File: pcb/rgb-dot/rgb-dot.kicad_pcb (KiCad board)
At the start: 2 copper layers, 7.6 x 8.9 mm, 4 parts, among them J1 HEADER-1x03, J2 HEADER-1x03, U1 WS2812B

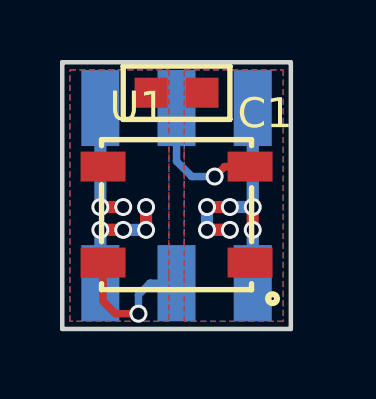
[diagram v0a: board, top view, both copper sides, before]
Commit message: Updated PCB pc-01 pc-02, Added display base pcb (pc-03, pc-04)
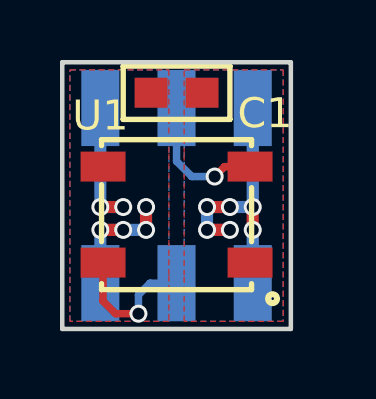
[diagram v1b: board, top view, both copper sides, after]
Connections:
- net Net-(J1-Pad2) renamed /DIN
- net Net-(J2-Pad2) renamed /DOUT
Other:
- board text added: "+"
- board text added: "-"
- board text added: "O-I"
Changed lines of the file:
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@@
-(kicad_pcb (version 4) (host pcbnew "(2015-05-27 BZR 5688)-product")
+(kicad_pcb (version 4) (host pcbnew "(2015-08-16 BZR 6095)-product")
   (general
     (links 8)
     (no_connects 0)
-    (area 142.936476 96.947 154.243524 112.042)
+    (area 144.704999 99.746999 152.475001 108.787001)
     (thickness 0.8)
-    (drawings 14)
+    (drawings 17)
     (tracks 38)
     (zones 0)
@@
   (net 0 "")
   (net 1 +5V)
-  (net 2 "Net-(J1-Pad2)")
-  (net 3 GND)
-  (net 4 "Net-(J2-Pad2)")
+  (net 2 GND)
+  (net 3 /DIN)
+  (net 4 /DOUT)
   (net_class Default "This is the default net class."
     (clearance 0.254)
@@
     (uvia_dia 0.3)
     (uvia_drill 0.1)
-    (add_net "Net-(J1-Pad2)")
-    (add_net "Net-(J2-Pad2)")
+    (add_net /DIN)
+    (add_net /DOUT)
   )
   (net_class Power ""
@@
       (net 1 +5V))
     (pad 2 smd rect (at 0 0) (size 1.27 2.54) (layers B.Cu B.Paste B.Mask)
-      (net 2 "Net-(J1-Pad2)"))
+      (net 3 /DIN))
     (pad 3 smd rect (at 2.54 0) (size 1.27 2.54) (layers B.Cu B.Paste B.Mask)
-      (net 3 GND))
+      (net 2 GND))
   )
   (module Conn-Wire-Pads:WP-50mil-1x03 (layer B.Cu)
@@
       (net 1 +5V))
     (pad 2 smd rect (at 0 0) (size 1.27 2.54) (layers B.Cu B.Paste B.Mask)
-      (net 4 "Net-(J2-Pad2)"))
+      (net 4 /DOUT))
     (pad 3 smd rect (at 2.54 0) (size 1.27 2.54) (layers B.Cu B.Paste B.Mask)
-      (net 3 GND))
+      (net 2 GND))
   )
   (module SMT:LED-5050 (layer F.Cu)
     (at 148.59 104.902)
-    (fp_text reference U1 (at -1.3 -3.6) (layer F.SilkS)
+    (fp_text reference U1 (at -2.54 -3.302) (layer F.SilkS)
       (effects (font (size 1 1) (thickness 0.18)))
     )
@@
     (fp_line (start -2.5 -1) (end -2.5 0.9) (layer F.SilkS) (width 0.18))
     (pad 2 smd rect (at -2.45 1.6) (size 1.5 1) (layers F.Cu F.Paste F.Mask)
-      (net 4 "Net-(J2-Pad2)"))
+      (net 4 /DOUT))
     (pad 3 smd rect (at 2.45 1.6) (size 1.5 1) (layers F.Cu F.Paste F.Mask)
-      (net 3 GND))
+      (net 2 GND))
     (pad 4 smd rect (at 2.45 -1.6) (size 1.5 1) (layers F.Cu F.Paste F.Mask)
-      (net 2 "Net-(J1-Pad2)"))
+      (net 3 /DIN))
     (pad 1 smd rect (at -2.45 -1.6) (size 1.5 1) (layers F.Cu F.Paste F.Mask)
       (net 1 +5V))
@@
     (fp_line (start -1.778 0.889) (end -1.778 -0.889) (layer F.SilkS) (width 0.18))
     (pad 1 smd rect (at -0.85 0 180) (size 1.1 1) (layers F.Cu F.Paste F.Mask)
-      (net 3 GND))
+      (net 2 GND))
     (pad 2 smd rect (at 0.85 0 180) (size 1.1 1) (layers F.Cu F.Paste F.Mask)
       (net 1 +5V))
@@
       (rotate (xyz 0 0 0))
     )
+  )
+  (gr_text - (at 151.13 103.505) (layer B.SilkS)
+    (effects (font (size 1.5 1.5) (thickness 0.3)) (justify mirror))
+  )
+  (gr_text + (at 146.05 103.505) (layer B.SilkS)
+    (effects (font (size 1.5 1.5) (thickness 0.3)) (justify mirror))
+  )
+  (gr_text O-I (at 148.59 104.14 270) (layer B.SilkS)
+    (effects (font (size 1 1) (thickness 0.25)) (justify mirror))
   )
   (gr_line (start 152.146 101.6) (end 150.876 101.6) (angle 90) (layer Eco2.User) (width 0.2))
@@
   (segment (start 146.05 104.648) (end 146.05 101.346) (width 0.4064) (layer B.Cu) (net 1))
   (segment (start 146.05 105.41) (end 146.05 107.188) (width 0.4064) (layer B.Cu) (net 1))
-  (via (at 149.86 103.632) (size 0.6) (drill 0.4) (layers F.Cu B.Cu) (net 2))
-  (segment (start 150.19 103.302) (end 149.86 103.632) (width 0.25) (layer F.Cu) (net 2))
-  (segment (start 151.04 103.302) (end 150.19 103.302) (width 0.25) (layer F.Cu) (net 2))
-  (segment (start 149.098 103.632) (end 149.86 103.632) (width 0.25) (layer B.Cu) (net 2))
-  (segment (start 148.59 103.124) (end 149.098 103.632) (width 0.25) (layer B.Cu) (net 2))
-  (segment (start 148.59 101.346) (end 148.59 103.124) (width 0.25) (layer B.Cu) (net 2))
-  (via (at 151.13 105.41) (size 0.6) (drill 0.4) (layers F.Cu B.Cu) (net 3))
-  (via (at 151.13 104.648) (size 0.6) (drill 0.4) (layers F.Cu B.Cu) (net 3))
-  (segment (start 151.13 105.41) (end 151.13 104.648) (width 0.4064) (layer F.Cu) (net 3))
-  (via (at 150.368 104.648) (size 0.6) (drill 0.4) (layers F.Cu B.Cu) (net 3))
-  (segment (start 151.13 104.648) (end 150.368 104.648) (width 0.4064) (layer B.Cu) (net 3))
-  (via (at 149.606 104.648) (size 0.6) (drill 0.4) (layers F.Cu B.Cu) (net 3))
-  (segment (start 150.368 104.648) (end 149.606 104.648) (width 0.4064) (layer F.Cu) (net 3))
-  (via (at 149.606 105.41) (size 0.6) (drill 0.4) (layers F.Cu B.Cu) (net 3))
-  (segment (start 149.606 104.648) (end 149.606 105.41) (width 0.4064) (layer B.Cu) (net 3))
-  (via (at 150.368 105.41) (size 0.6) (drill 0.4) (layers F.Cu B.Cu) (net 3))
-  (segment (start 149.606 105.41) (end 150.368 105.41) (width 0.4064) (layer F.Cu) (net 3))
-  (segment (start 151.13 101.346) (end 151.13 104.648) (width 0.4064) (layer B.Cu) (net 3))
-  (segment (start 151.13 105.41) (end 151.13 107.188) (width 0.4064) (layer B.Cu) (net 3))
+  (via (at 151.13 105.41) (size 0.6) (drill 0.4) (layers F.Cu B.Cu) (net 2))
+  (via (at 151.13 104.648) (size 0.6) (drill 0.4) (layers F.Cu B.Cu) (net 2))
+  (segment (start 151.13 105.41) (end 151.13 104.648) (width 0.4064) (layer F.Cu) (net 2))
+  (via (at 150.368 104.648) (size 0.6) (drill 0.4) (layers F.Cu B.Cu) (net 2))
+  (segment (start 151.13 104.648) (end 150.368 104.648) (width 0.4064) (layer B.Cu) (net 2))
+  (via (at 149.606 104.648) (size 0.6) (drill 0.4) (layers F.Cu B.Cu) (net 2))
+  (segment (start 150.368 104.648) (end 149.606 104.648) (width 0.4064) (layer F.Cu) (net 2))
+  (via (at 149.606 105.41) (size 0.6) (drill 0.4) (layers F.Cu B.Cu) (net 2))
+  (segment (start 149.606 104.648) (end 149.606 105.41) (width 0.4064) (layer B.Cu) (net 2))
+  (via (at 150.368 105.41) (size 0.6) (drill 0.4) (layers F.Cu B.Cu) (net 2))
+  (segment (start 149.606 105.41) (end 150.368 105.41) (width 0.4064) (layer F.Cu) (net 2))
+  (segment (start 151.13 101.346) (end 151.13 104.648) (width 0.4064) (layer B.Cu) (net 2))
+  (segment (start 151.13 105.41) (end 151.13 107.188) (width 0.4064) (layer B.Cu) (net 2))
+  (via (at 149.86 103.632) (size 0.6) (drill 0.4) (layers F.Cu B.Cu) (net 3))
+  (segment (start 150.19 103.302) (end 149.86 103.632) (width 0.25) (layer F.Cu) (net 3))
+  (segment (start 151.04 103.302) (end 150.19 103.302) (width 0.25) (layer F.Cu) (net 3))
+  (segment (start 149.098 103.632) (end 149.86 103.632) (width 0.25) (layer B.Cu) (net 3))
+  (segment (start 148.59 103.124) (end 149.098 103.632) (width 0.25) (layer B.Cu) (net 3))
+  (segment (start 148.59 101.346) (end 148.59 103.124) (width 0.25) (layer B.Cu) (net 3))
   (via (at 147.32 108.204) (size 0.6) (drill 0.4) (layers F.Cu B.Cu) (net 4))
   (segment (start 147.32 108.204) (end 146.558 108.204) (width 0.25) (layer F.Cu) (net 4))
@@
     )
   )
-  (zone (net 3) (net_name GND) (layer F.Cu) (hatch edge 0.508)
+  (zone (net 2) (net_name GND) (layer F.Cu) (hatch edge 0.508)
     (connect_pads (clearance 0))
     (min_thickness 0.254)
@@
     )
   )
-  (zone (net 3) (net_name GND) (layer B.Cu) (hatch edge 0.508)
+  (zone (net 2) (net_name GND) (layer B.Cu) (hatch edge 0.508)
     (connect_pads (clearance 0))
     (min_thickness 0.254)

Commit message: Updated schematics
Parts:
- moved C1 7.15 mm to (149.4, 108.0), turned to 0 degrees
- moved J1 6.14 mm to (149.4, 107.4), turned to 180 degrees
- moved J2 5.64 mm to (149.4, 101.6), turned to 180 degrees
- moved U1 1.27 mm to (149.4, 103.9), turned to 180 degrees
